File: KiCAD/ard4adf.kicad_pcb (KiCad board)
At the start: 2 copper layers, 45 x 55.1 mm, 35 parts, among them IC1 ADM7150ARDZ-5.0, IC2 ADM7150ARDZ-3.3, J1 Conn_01x02_Male, J2 Conn_02x03_Odd_Even, J3 Conn_02x05_Top_Bottom, J4 Conn_01x04_Male, J5 Conn_01x02_Male, J6 Conn_01x02_Male

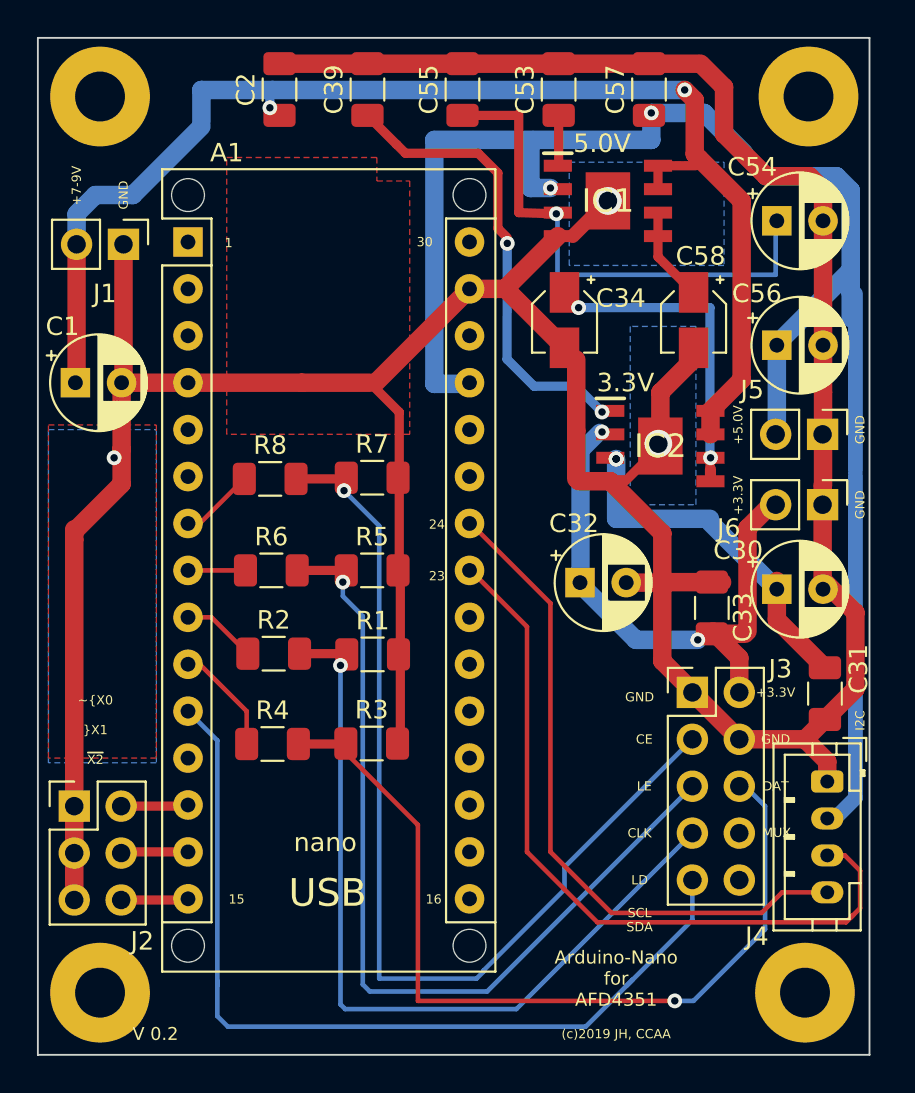
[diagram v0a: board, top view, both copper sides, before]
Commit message: Adds R(220) and output-pins J7 for external LED
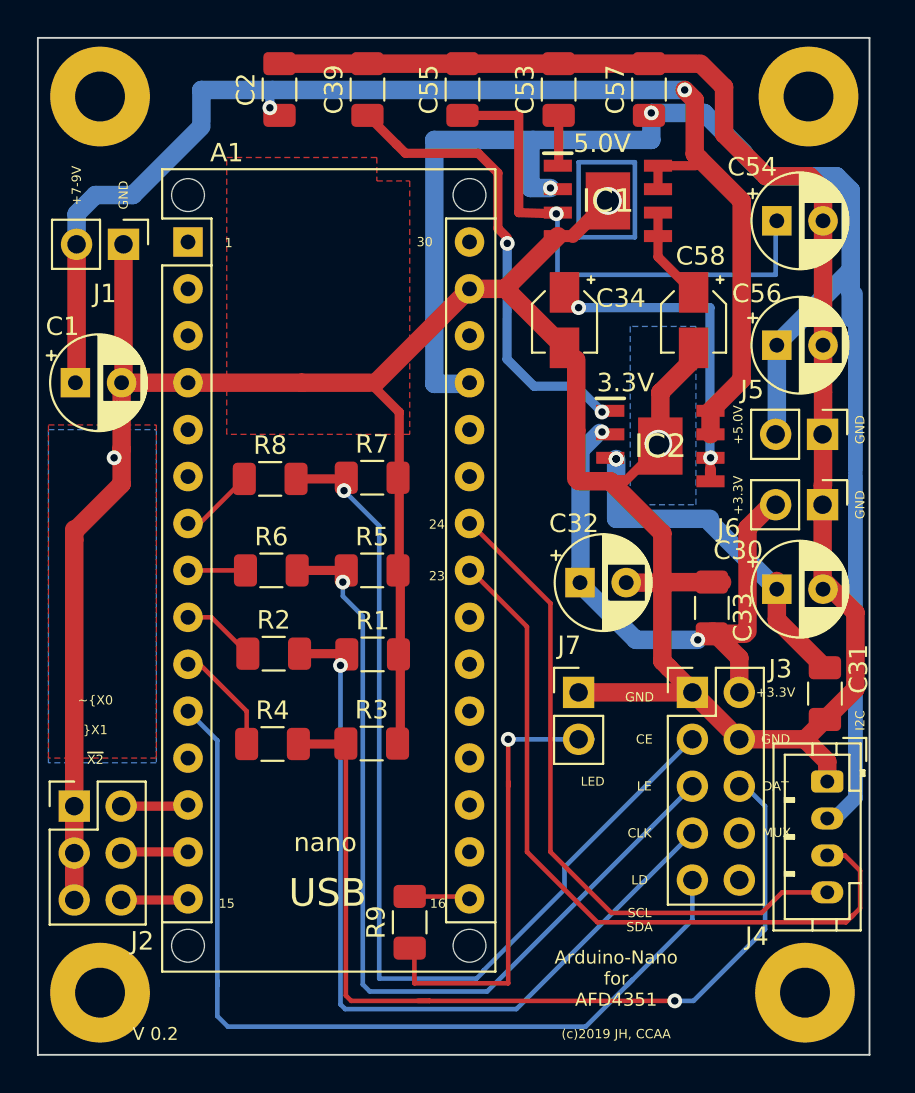
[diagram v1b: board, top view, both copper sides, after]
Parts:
- added J7: Conn_01x02_Male, Connector_PinHeader_2.54mm:PinHeader_1x02_P2.54mm_Vertical, F.Cu at (92.7, 111.8)
- added R9: 220, Resistor_SMD:R_1206_3216Metric, F.Cu at (83.6, 124.2)
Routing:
- net Net-(J7-Pad2): track 0.00 -> 25.0 mm, vias 0 -> 1
- net (no net): track 0.00 -> 14.2 mm
- net GND: track 215.4 -> 220.8 mm
- net Net-(A1-Pad16): track 0.00 -> 3.04 mm
- net Net-(J3-Pad6): track 46.9 -> 49.9 mm
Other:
- board text added: "LED"

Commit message: Updates PCB to newest order
Adds 5-pin connector: A0, D2, D3, D9
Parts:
- added J8: Conn_01x05_Male, Connector_PinHeader_2.54mm:PinHeader_1x05_P2.54mm_Vertical, F.Cu at (67.1, 98.3)
- added REF**: OSHW-Logo2_7.3x6mm_SilkScreen, Symbol:OSHW-Logo2_7.3x6mm_SilkScreen, B.Cu at (77.5, 121.7)
- added REF**: KiCad-Logo2_5mm_SilkScreen, Symbol:KiCad-Logo2_5mm_SilkScreen, B.Cu at (78.7, 90.4)
- IC2: footprint ADM7150ARDZ-3.3:SOIC127P600X175-9N -> SOIC127P600X175-9N
- moved C1 3.72 mm to (66.5, 91.4), turned to 270 degrees
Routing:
- net GND: track 220.8 -> 265.6 mm, vias 3 -> 4
- net Net-(A1-Pad19): track 0.00 -> 36.9 mm
- net (no net): track 14.2 -> 0.00 mm
- net Net-(A1-Pad12): track 0.00 -> 10.2 mm
- net Net-(A1-Pad6): track 0.00 -> 8.45 mm
- net Net-(A1-Pad5): track 0.00 -> 8.34 mm
- net Net-(C1-Pad1): track 71.5 -> 68.4 mm
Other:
- board text added: "A0"
- board text added: "D2"
- board text added: "D3"
- board text added: "D9"
- board text added: "X0 X1 X2"
- board text added: "v0.3"
- board text removed: "V 0.2"
- board text removed: "~X0 ~X1 ~X2"
